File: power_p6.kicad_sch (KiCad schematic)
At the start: 23 parts, among them J1 LSHM-140-04.0-L-DV-A-N-K-TR, U1 LT8624S

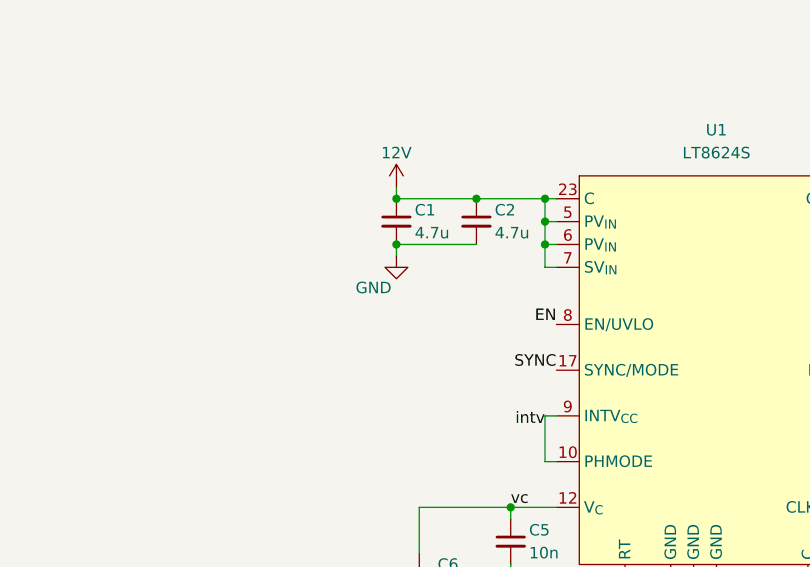
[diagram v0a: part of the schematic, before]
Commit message: Add input RC snubber
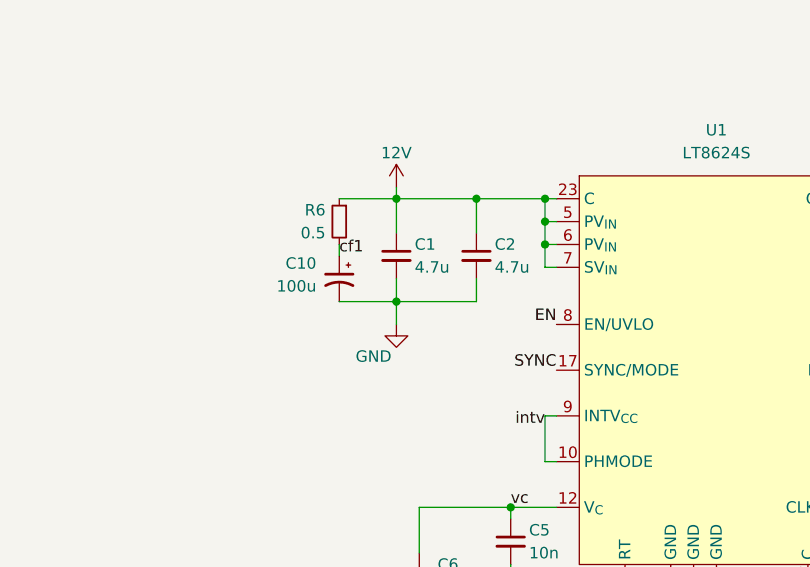
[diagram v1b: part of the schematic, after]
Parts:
- added C10: 100u, lib:T521X, symbol Device:C_Polarized_Small_US
- added R6: 0.5, Resistor_SMD:R_0603_1608Metric, symbol Device:R_Small
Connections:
- net 12V: now also R6.1
- net GND: now also C10.2
- new net cf1: C10.1, R6.2
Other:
- moved on the sheet: C1, C2

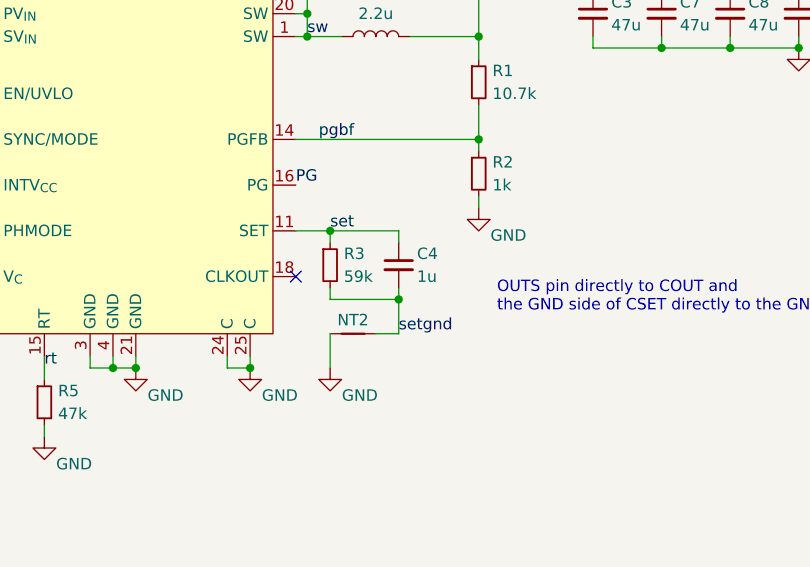
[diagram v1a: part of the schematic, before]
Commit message: update set resistor to thin film
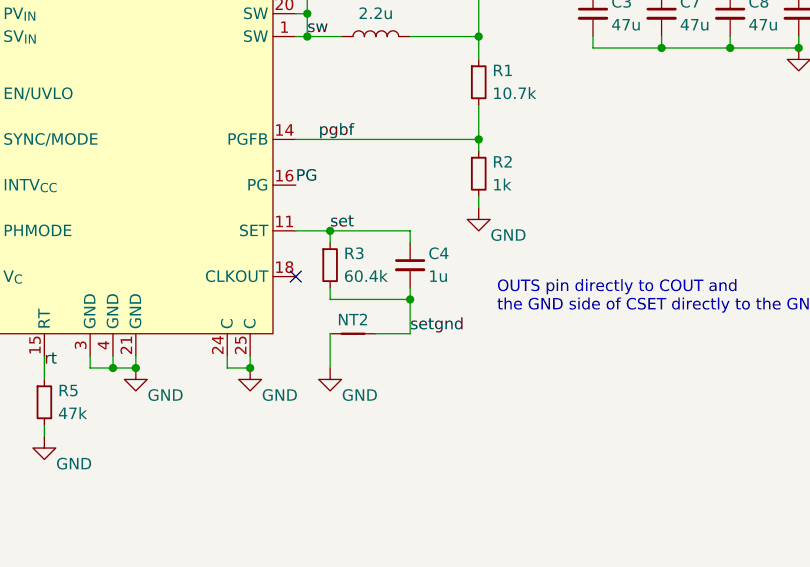
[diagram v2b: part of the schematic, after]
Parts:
- R3: value 59k -> 60.4k; M Vishay -> Panasonic; MPN CRCW060359K0FKEA -> ERA-3AEB6042V
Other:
- moved on the sheet: C4
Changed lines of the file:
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@@
 	)
 	(junction
+		(at 200.66 97.79)
+		(diameter 0)
+		(color 0 0 0 0)
+	)
+	(junction
 		(at 60.96 118.11)
 		(diameter 0)
@@
 	)
 	(junction
-		(at 199.39 97.79)
-		(diameter 0)
-		(color 0 0 0 0)
-	)
-	(junction
 		(at 60.96 92.71)
 		(diameter 0)
@@
 	(wire
 		(pts
-			(xy 191.77 97.79) (xy 199.39 97.79)
+			(xy 191.77 97.79) (xy 200.66 97.79)
 		)
 		(stroke
@@
 	(wire
 		(pts
-			(xy 196.85 101.6) (xy 199.39 101.6)
+			(xy 196.85 101.6) (xy 200.66 101.6)
 		)
 		(stroke
@@
 	(wire
 		(pts
-			(xy 199.39 96.52) (xy 199.39 97.79)
+			(xy 200.66 96.52) (xy 200.66 97.79)
 		)
 		(stroke
@@
 	(wire
 		(pts
-			(xy 199.39 91.44) (xy 199.39 90.17)
+			(xy 200.66 91.44) (xy 200.66 90.17)
 		)
 		(stroke
@@
 	(wire
 		(pts
-			(xy 191.77 90.17) (xy 199.39 90.17)
+			(xy 191.77 90.17) (xy 200.66 90.17)
 		)
 		(stroke
@@
 	(wire
 		(pts
-			(xy 199.39 97.79) (xy 199.39 101.6)
+			(xy 200.66 97.79) (xy 200.66 101.6)
 		)
 		(stroke
@@
 	)
 	(label "setgnd"
-		(at 199.39 101.6 0)
+		(at 200.66 101.6 0)
 		(effects
 			(font
@@
 			)
 		)
-		(property "Value" "59k"
+		(property "Value" "60.4k"
 			(at 193.294 95.25 0)
 			(effects
@@
 			)
 		)
-		(property "Description" "59 kOhms ±1% 0.1W, 1/10W Chip Resistor 0603 (1608 Metric) Automotive AEC-Q200 Thick Film"
-			(at 191.77 93.98 0)
-			(effects
-				(font
-					(size 1.27 1.27)
-				)
-				(hide yes)
-			)
-		)
-		(property "M" "Vishay"
+		(property "Description" "60.4 kOhms ±0.1% 0.1W, 1/10W Chip Resistor 0603 (1608 Metric) Automotive AEC-Q200 Thin Film"
 			(at 191.77 93.98 0)
 			(effects
@@
 			)
 		)
-		(property "MPN" "CRCW060359K0FKEA"
+		(property "M" "Panasonic"
 			(at 191.77 93.98 0)
 			(effects
@@
 			)
 		)
-		(property "Field6" ""
+		(property "MPN" "ERA-3AEB6042V"
 			(at 191.77 93.98 0)
 			(effects
@@
 	(symbol
 		(lib_id "Device:C_Small")
-		(at 199.39 93.98 0)
+		(at 200.66 93.98 0)
 		(unit 1)
 		(exclude_from_sim no)
@@
 		(dnp no)
 		(property "Reference" "C4"
-			(at 201.422 92.71 0)
+			(at 202.692 92.71 0)
 			(effects
 				(font
@@
 		)
 		(property "Value" "1u"
-			(at 201.422 95.25 0)
+			(at 202.692 95.25 0)
 			(effects
 				(font
@@
 		)
 		(property "Footprint" "Capacitor_SMD:C_0603_1608Metric"
-			(at 199.39 93.98 0)
+			(at 200.66 93.98 0)
 			(effects
 				(font
@@
 		)
 		(property "Datasheet" "~"
-			(at 199.39 93.98 0)
+			(at 200.66 93.98 0)
 			(effects
 				(font
@@
 		)
 		(property "Description" "1 µF ±10% 25V Ceramic Capacitor X7R 0603 (1608 Metric)"
-			(at 199.39 93.98 0)
+			(at 200.66 93.98 0)
 			(effects
 				(font
@@
 		)
 		(property "M" "Murata"
-			(at 199.39 93.98 0)
+			(at 200.66 93.98 0)
 			(effects
 				(font
@@
 		)
 		(property "MPN" "GCM188R71E105KA64D"
-			(at 199.39 93.98 0)
+			(at 200.66 93.98 0)
 			(effects
 				(font
@@
 		)
 		(property "Field6" ""
-			(at 199.39 93.98 0)
+			(at 200.66 93.98 0)
 			(effects
 				(font
